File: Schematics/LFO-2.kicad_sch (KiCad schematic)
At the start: 58 parts, among them J66 Conn_01x10h, J67 Conn_01x05, J68 Conn_01x04, J69 Conn_01x03, U118 LM78L05, U79 LM358, U80 ADG419BN, U81 LM358, U82 LM324, U84 SSI2130, U85 LM324

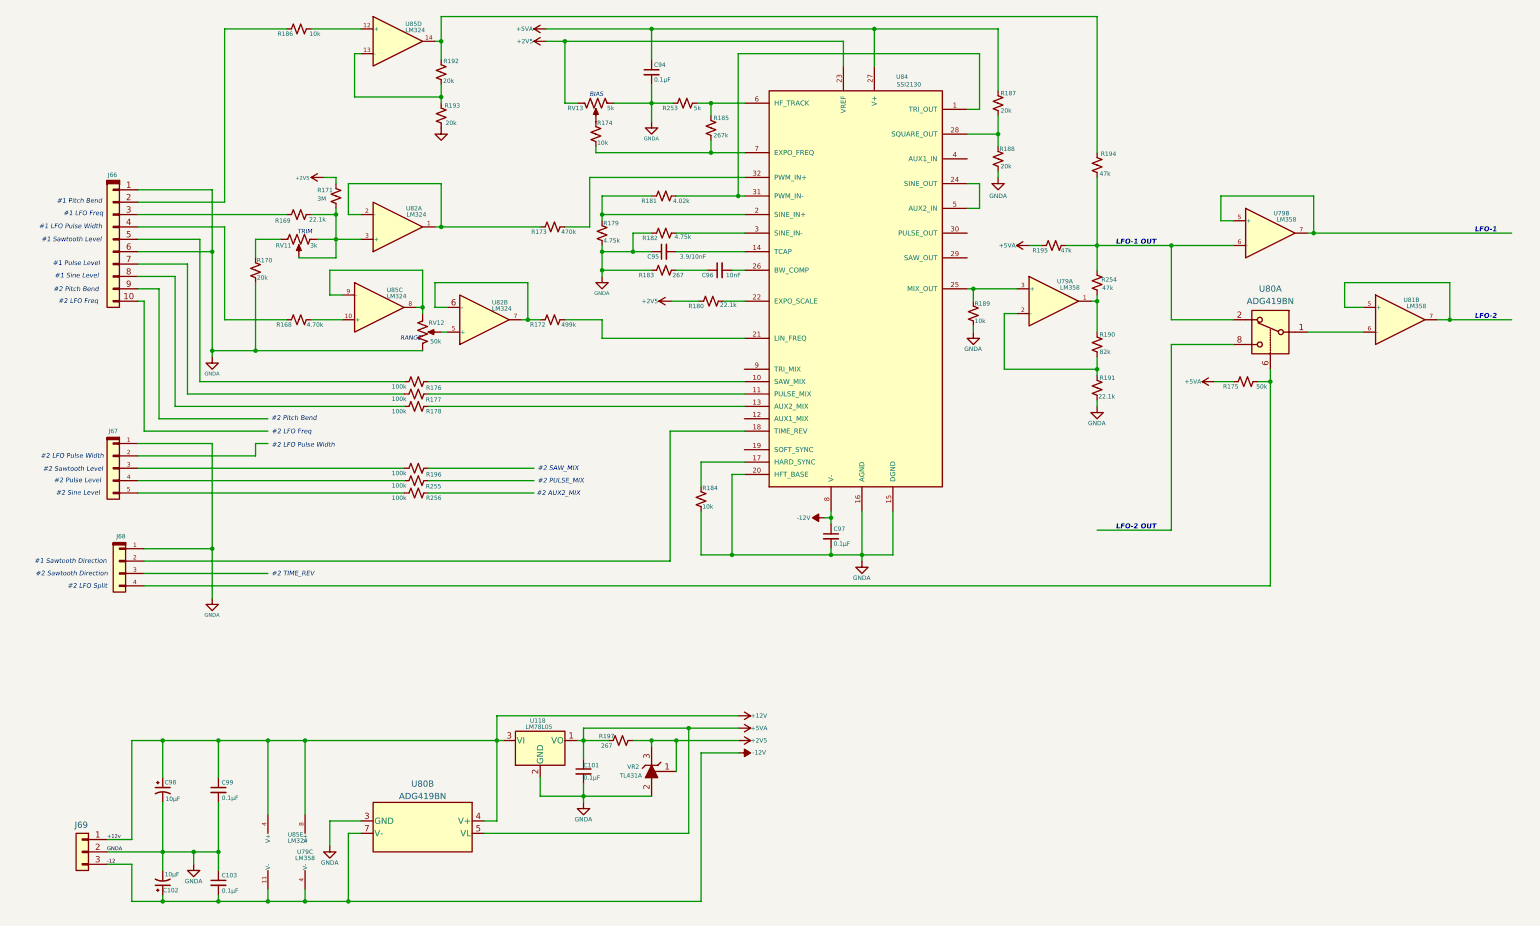
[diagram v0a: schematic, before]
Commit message: Upgreade byte value interface to short.  First stage of refactoring midi input for rotory encoders.  Still needs scaling.
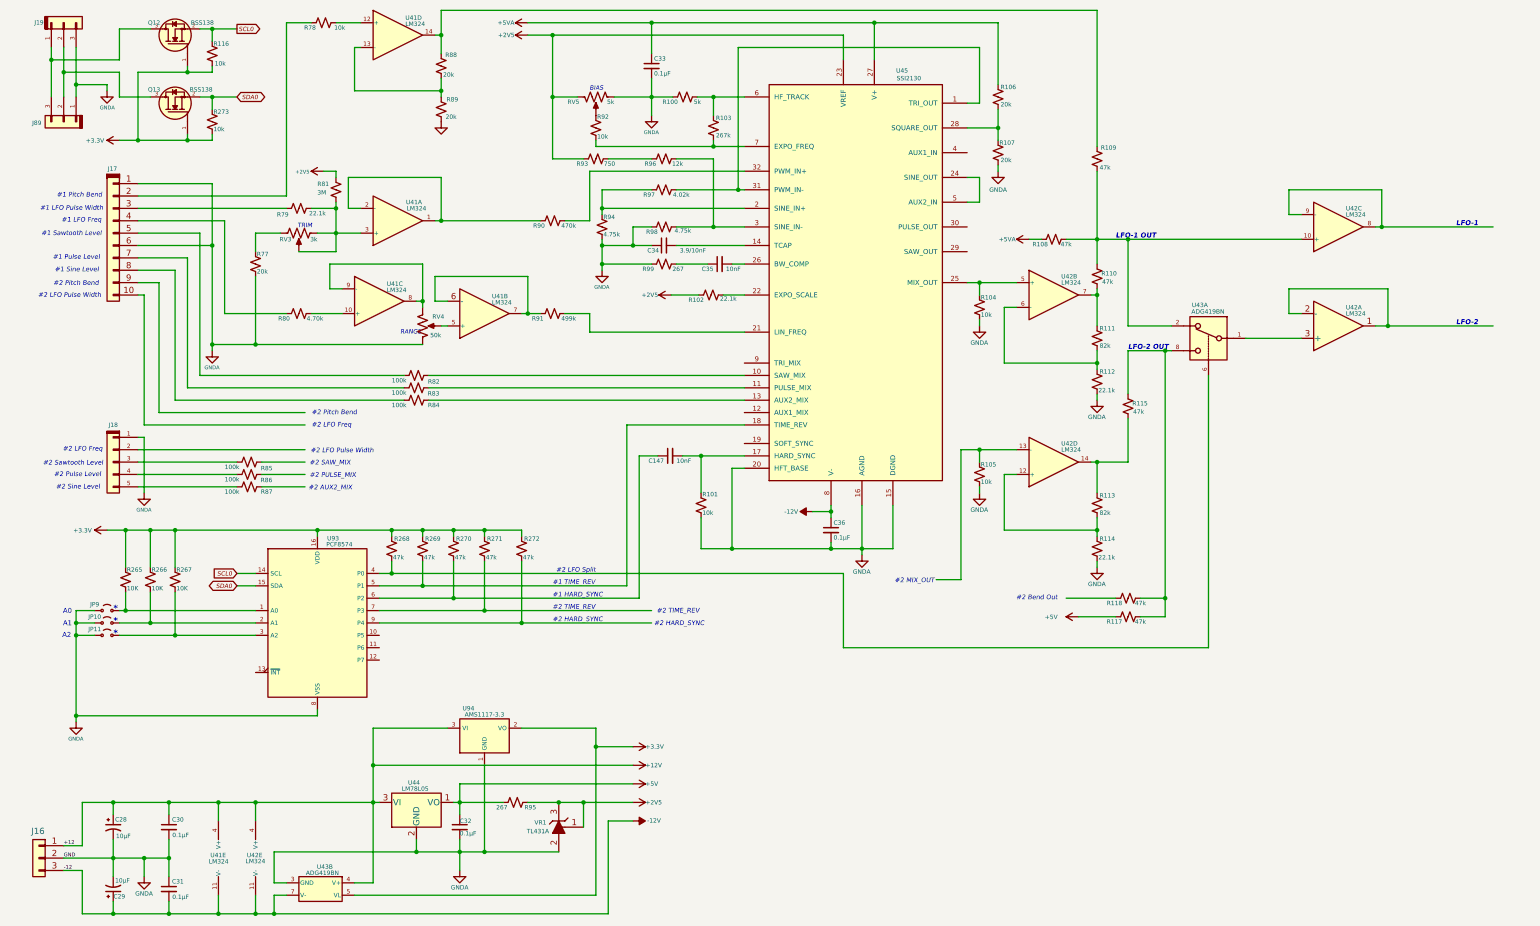
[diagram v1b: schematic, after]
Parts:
- removed J68: Conn_01x04, symbol My Connectors:Conn_01x04
- removed R175: 50k, symbol Device:R_Small_US
- removed U79, U81: LM358, symbol Amplifier_Operational:LM358
- added C147: 10nF, symbol Device:C_Small
- added J19, J89: Conn_01x03, symbol My Connectors:Conn_01x03
- added JP10, JP11, JP9: Jumper_2_Small_Open, symbol Jumper:Jumper_2_Small_Open
- added Q12, Q13: BSS138, digikey-footprints:SOT-23-3, symbol dk_Transistors-FETs-MOSFETs-Single:BSS138
- added R105, R116, R273: 10k, symbol Device:R_Small_US
- added R113: 82k, symbol Device:R_Small_US
- added R114: 22.1k, symbol Device:R_Small_US
- added R115, R117, R118, R268, R269, R270, R271, R272: 47k, symbol Device:R_Small_US
- added R265, R266, R267: 10K, symbol Device:R_Small_US
- added R93: 750, symbol Device:R_Small_US
- added R96: 12k, symbol Device:R_Small_US
- added U42: LM324, symbol Amplifier_Operational:LM324
- added U93: PCF8574, symbol Interface_Expansion:PCF8574
- added U94: AMS1117-3.3, Package_TO_SOT_SMD:SOT-223-3_TabPin2, symbol Regulator_Linear:AMS1117-3.3
- renumbered C98 to C28, C102 to C29, C99 to C30, C103 to C31, C101 to C32, C94 to C33, C95 to C34, C96 to C35, C97 to C36, J69 to J16, J66 to J17, J67 to J18, R253 to R100, R184 to R101, R180 to R102, R185 to R103, R189 to R104, R187 to R106, R188 to R107, R195 to R108, R194 to R109, R254 to R110, R190 to R111, R191 to R112, R170 to R77, R186 to R78, R169 to R79, R168 to R80, R171 to R81, R176 to R82, R177 to R83, R178 to R84, R196 to R85, R255 to R86, R256 to R87, R192 to R88, R193 to R89, R173 to R90, R172 to R91, R174 to R92, R179 to R94, R197 to R95, R181 to R97, R182 to R98, R183 to R99, RV11 to RV3, RV12 to RV4, RV13 to RV5, U85 to U41, U82 to U41, U80 to U43, U118 to U44, U84 to U45, VR2 to VR1
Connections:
- net +12V: now also U42.4 (V+), U94.3 (VI)
- net +2V5: now also R93.1
- net +5VA: no longer C32.1, R95.1, U43.5 (VL), U44.1 (VO)
- net -12V: now also U42.11 (V-)
- net GNDA: now also J19.3 (Pin_3), J89.1 (Pin_1), JP10.1 (A), JP11.1 (A), JP9.1 (A), R105.2, R114.2, U93.8 (VSS), U94.1 (GND)
- net at R110.2, R111.1: now also U42.7
- net at R111.2, R112.1: now also U42.6 (-)
- net at R104.1, U45.25 (MIX_OUT): now also U42.5 (+)
- net at R101.1, U45.17 (HARD_SYNC): now also C147.2
- net at U45.18 (TIME_REV): now also R269.2, U93.5 (P1)
- net at R98.2, U45.3 (SINE_IN-): now also R96.2
- net at U43.1: now also U42.3 (+)
- net at R108.2, R109.2, R110.1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: now also U42.10 (+)
- net at U43.6: now also R268.2, U93.4 (P0)
- net at U43.8: now also R115.1, R117.2, R118.2
- new net: R113.2, R114.1, U42.12 (+)
- new net: R105.1, U42.13 (-)
- new net: R113.1, R115.2, U42.14
- new net: R271.2, U93.7 (P3)
- new net: J19.2 (Pin_2), J89.2 (Pin_2), Q13.3
- new net: J19.1 (Pin_1), J89.3 (Pin_3), Q12.3
- new net: C147.1, R270.2, U93.6 (P2)
- new net: JP10.2 (B), R266.2, U93.2 (A1)
- new net: U42.8, U42.9 (-)
- new net: R272.2, U93.9 (P4)
- new net: JP11.2 (B), R267.2, U93.3 (A2)
- new net: U42.1, U42.2 (-)
- new net: JP9.2 (B), R265.2, U93.1 (A0)
- new net: R93.2, R96.1
- new net +3.3V: Q12.1, Q13.1, R116.2, R265.1, R266.1, R267.1, R268.1, R269.1, R270.1, R271.1, R272.1, R273.2, U43.5 (VL), U93.16 (VDD), U94.2 (VO)
- new net +5V: C32.1, R117.1, R95.1, U44.1 (VO)
- new net SCL0: Q12.2, R116.1, U93.14 (SCL)
- new net SDA0: Q13.2, R273.1, U93.15 (SDA)
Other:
- note added: "#1 HARD_SYNC"
- note added: "#1 TIME_REV"
- note added: "#2 Bend Out"
- note added: "#2 HARD_SYNC"
- note added: "#2 MIX_OUT"
- note added: "*"
- note added: "A0"
- note added: "A1"
- note added: "A2"
- note removed: "#1 Sawtooth Direction"
- note removed: "#2 Sawtooth Direction"
- moved on the sheet: C28, C29, C30, C31, C32, C33, C34, C35, C36, J16, J17, J18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

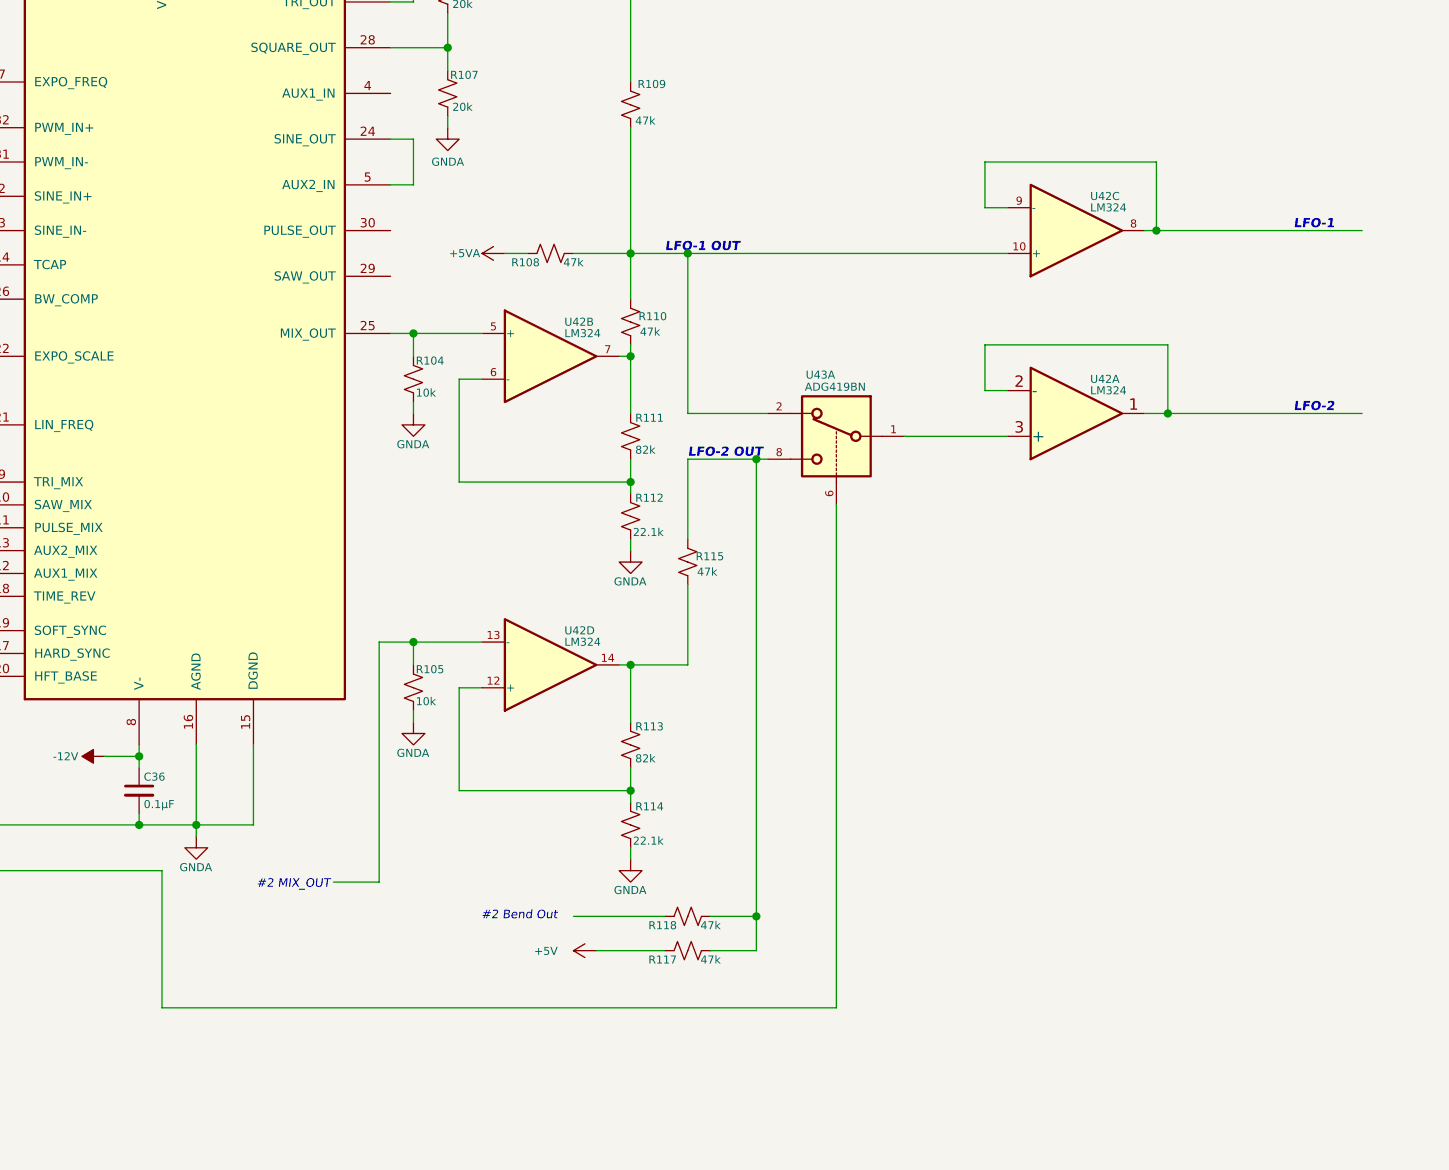
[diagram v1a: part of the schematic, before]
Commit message: Adding in partion LFO-2.  Changed keboard buttons to momentary and encoders to just direction.
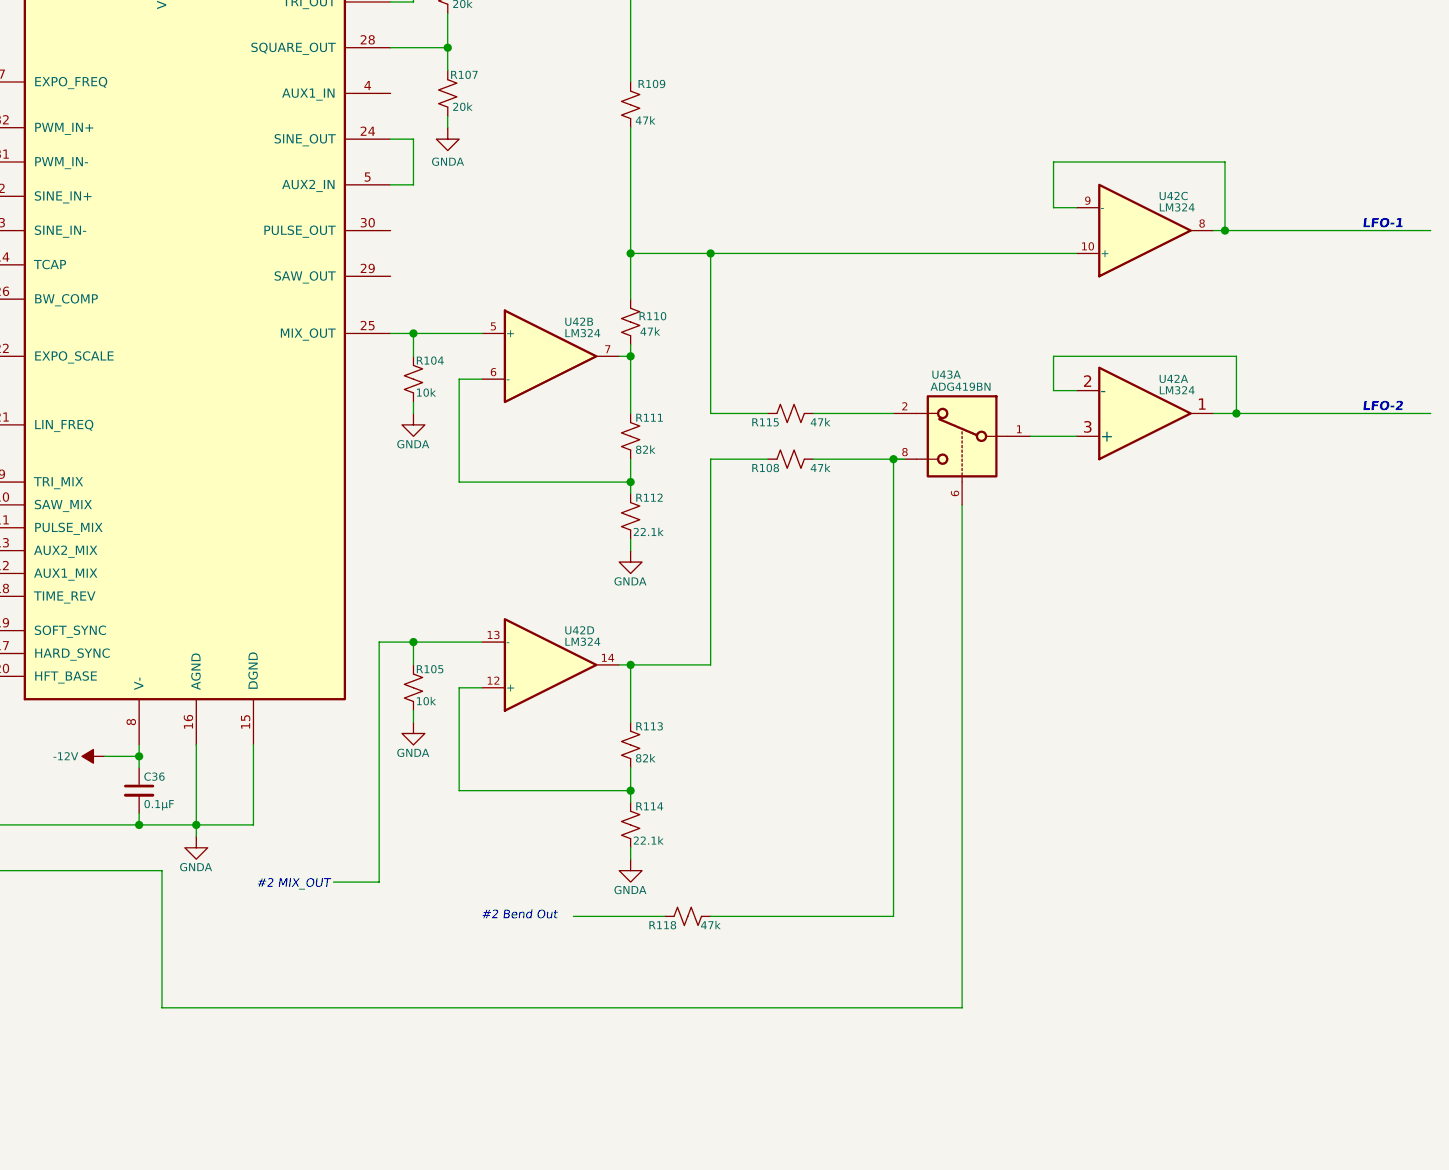
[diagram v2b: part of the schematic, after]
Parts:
- removed R117: 47k, symbol Device:R_Small_US
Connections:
- net +5VA: no longer R108.1
- net at R113.1, U42.14: now also R108.1; no longer R115.2
- net at R118.2, U43.8: now also R108.2; no longer R115.1
- net at R109.2, R110.1, U42.10 (+): now also R115.1; no longer R108.2, U43.2
- new net: R115.2, U43.2
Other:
- note removed: "LFO-1 OUT"
- note removed: "LFO-2 OUT"
- moved on the sheet: U42A, U42C, U43A

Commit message: Updated schematics including VCO and VCF daughter boards
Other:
- company:       MLE Tech                  Cedar Park, TX -> (none)
- title: Synth #2 -> Dual LFO
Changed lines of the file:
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@@
 	(paper "USLegal")
 	(title_block
-		(title "Synth #2")
-		(date "2023-07-27")
-		(rev "0.1")
-		(company "      MLE Tech                  Cedar Park, TX")
-		(comment 2 "In Development")
+		(title "Dual LFO")
+		(date "2025-01-16")
+		(rev "2.4")
+		(comment 1 "In Development ")
 	)
 	(junction

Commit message: Final tweaks on LFO interfaces and tuning.  Update display layouts.
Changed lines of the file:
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@@
 	(text "#2 LFO Freq"
 		(exclude_from_sim no)
-		(at 73.7288 101.0277 0)
+		(at 73.2024 106.0904 0)
 		(effects
 			(font
@@
 	(text "#2 LFO Pulse Width"
 		(exclude_from_sim no)
-		(at 73.5116 106.2984 0)
-		(effects
-			(font
+		(at 73.4349 101.2092 0)
+		(effects
+			(font
